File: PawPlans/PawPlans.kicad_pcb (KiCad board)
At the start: 2 copper layers, 80 x 66 mm, 7 parts

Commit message: Completely revamped the schematic and PCB, cleaned up project files
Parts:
- removed LOAD-CELL1: SEN-13879, Parts:SPARKFUN_SEN-13879
- removed PROXIMITY-SENSOR1: ~, Ultrasonic Sensor HC-SR04:HC-SR04_FOOTPRINT
- added LOADCELL1: ~, SparkFun_HX711_Load_Cell_Amplifier_SEN-13879:SPARKFUN-CONNECTORS_1X05, F.Cu at (83.7, 66.3)
- added PROXIMITY1: ~, Ultrasonic_Proximity_Sensor_HC-SR04:HC-SR04_FOOTPRINT, F.Cu at (115.8, 66.0)
- BUZZER1: footprint Parts:XTAL_PS1240P02BT_TDK -> TDK_Piezo_Buzzer_PS1240P02BT:XTAL_PS1240P02BT_TDK
- DISPLAY1: renamed from OLED-BREAKOUT1; footprint Qwiic_OLED_1.3in:SPARKX_1X04_NO_SILK -> SparkFun_Qwiic_OLED_128x64_LCD-23453:SPARKX_1X04
- JOYSTICK1: footprint Parts:1X05 -> Adafruit_Joystick_512:PINHEAD_1X05
- MCUKIT1: renamed from WIFI-DEVKIT1; footprint Espressif:ESP32-C6-DevKitC-1 -> Espressif_ESP32:ESP32-C6-DevKitC-1
- SERVO1: footprint Motors:Vybronics_VZ30C1T8219732L -> Connector_PinHeader_2.00mm:PinHeader_1x03_P2.00mm_Vertical
- moved BUZZER1 98.4 mm to (115.6, 36.8)
- moved MCUKIT1 69.2 mm to (88.2, 43.8)
- moved JOYSTICK1 68.9 mm to (115.7, 53.0), turned to -90 degrees
- moved DISPLAY1 58.5 mm to (83.7, 52.1), turned to 90 degrees
- moved SERVO1 48.6 mm to (115.7, 74.0)
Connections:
- net Net-(OLED-BREAKOUT1-SCL) renamed /DSPSCL
- net Net-(OLED-BREAKOUT1-SDA) renamed /DSPSDA
- BUZZER1 pad 1: Net-(WIFI-DEVKIT1-GPIO12/USB_D-) -> /PZOSIG
- JOYSTICK1 pad 2: Net-(WIFI-DEVKIT1-GPIO16/U0TXD) -> /JOYX
- JOYSTICK1 pad 3: Net-(WIFI-DEVKIT1-GPIO17/U0RXD) -> /JOYY
- JOYSTICK1 pad 4: Net-(WIFI-DEVKIT1-GPIO15/JTAG) -> /JOYSEL
- MCUKIT1 pad 12: Net-(SERVO1-PWM) -> unconnected-(MCUKIT1-GPIO2-Pad12)
- MCUKIT1 pad 19: Net-(WIFI-DEVKIT1-GPIO12/USB_D-) -> unconnected-(MCUKIT1-GPIO12/USB_D--Pad19)
- MCUKIT1 pad 20: Net-(WIFI-DEVKIT1-GPIO13/USB_D+) -> unconnected-(MCUKIT1-GPIO13/USB_D+-Pad20)
- MCUKIT1 pad 22: Net-(WIFI-DEVKIT1-GPIO9/BOOT) -> /SRVPWM
- MCUKIT1 pad 24: unconnected-(WIFI-DEVKIT1-GPIO19-Pad24) -> /PRXTRG
- MCUKIT1 pad 25: unconnected-(WIFI-DEVKIT1-GPIO20-Pad25) -> /PRXECH
- MCUKIT1 pad 26: unconnected-(WIFI-DEVKIT1-GPIO21-Pad26) -> /JOYSEL
- MCUKIT1 pad 27: unconnected-(WIFI-DEVKIT1-GPIO22-Pad27) -> /JOYY
- MCUKIT1 pad 28: unconnected-(WIFI-DEVKIT1-GPIO23-Pad28) -> /JOYX
- MCUKIT1 pad 29: Net-(WIFI-DEVKIT1-GPIO15/JTAG) -> unconnected-(MCUKIT1-GPIO15/JTAG-Pad29)
- MCUKIT1 pad 30: Net-(WIFI-DEVKIT1-GPIO17/U0RXD) -> unconnected-(MCUKIT1-GPIO17/U0RXD-Pad30)
- MCUKIT1 pad 31: Net-(WIFI-DEVKIT1-GPIO16/U0TXD) -> /PZOSIG
- MCUKIT1 pad 6: Net-(LOAD-CELL1-CLK) -> /LDCCLK
- MCUKIT1 pad 7: Net-(LOAD-CELL1-DAT) -> /LDCDAT
- SERVO1 pad 1: Net-(SERVO1-PWM) -> /SRVPWM
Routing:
- net Net-(WIFI-DEVKIT1-GPIO15/JTAG): track 13.0 -> 0.00 mm
- net /PZOSIG: track 0.00 -> 11.5 mm
- net Net-(WIFI-DEVKIT1-GPIO13/USB_D+): track 10.5 -> 0.00 mm
- net Net-(LOAD-CELL1-CLK): track 10.2 -> 0.00 mm
- net Net-(WIFI-DEVKIT1-GPIO17/U0RXD): track 9.42 -> 0.00 mm
- net Net-(SERVO1-PWM): track 9.19 -> 0.00 mm
- net /VCC: track 59.8 -> 51.5 mm
- net /DSPSDA: track 14.0 -> 6.26 mm
- net Net-(WIFI-DEVKIT1-GPIO12/USB_D-): track 7.55 -> 0.00 mm
- net Net-(WIFI-DEVKIT1-GPIO9/BOOT): track 6.97 -> 0.00 mm
- net Net-(WIFI-DEVKIT1-GPIO16/U0TXD): track 6.89 -> 0.00 mm
- net /SRVPWM: track 0.00 -> 6.69 mm
- net /JOYX: track 0.00 -> 6.15 mm
- net /JOYY: track 0.00 -> 6.15 mm
- net /JOYSEL: track 0.00 -> 6.15 mm
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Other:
- board size 80 x 66 mm -> 48 x 68 mm

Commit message: Added board title and credits to silkscreen
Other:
- board text added: "PawPlans - Automatic Pet Feeder v0.5.0 Sriram Vishnubhotla, Logan Swoyer, Jacob Sorber Clemson University"
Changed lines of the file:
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@@
 		(layer "Edge.Cuts")
+	)
+	(gr_text "PawPlans - Automatic Pet Feeder v0.5.0\nSriram Vishnubhotla, Logan Swoyer, Jacob Sorber\nClemson University"
+		(at 89.6 31.2 0)
+		(layer "F.SilkS")
+		(effects
+			(font
+				(size 0.5 0.5)
+				(thickness 0.0625)
+			)
+		)
 	)
 	(segment

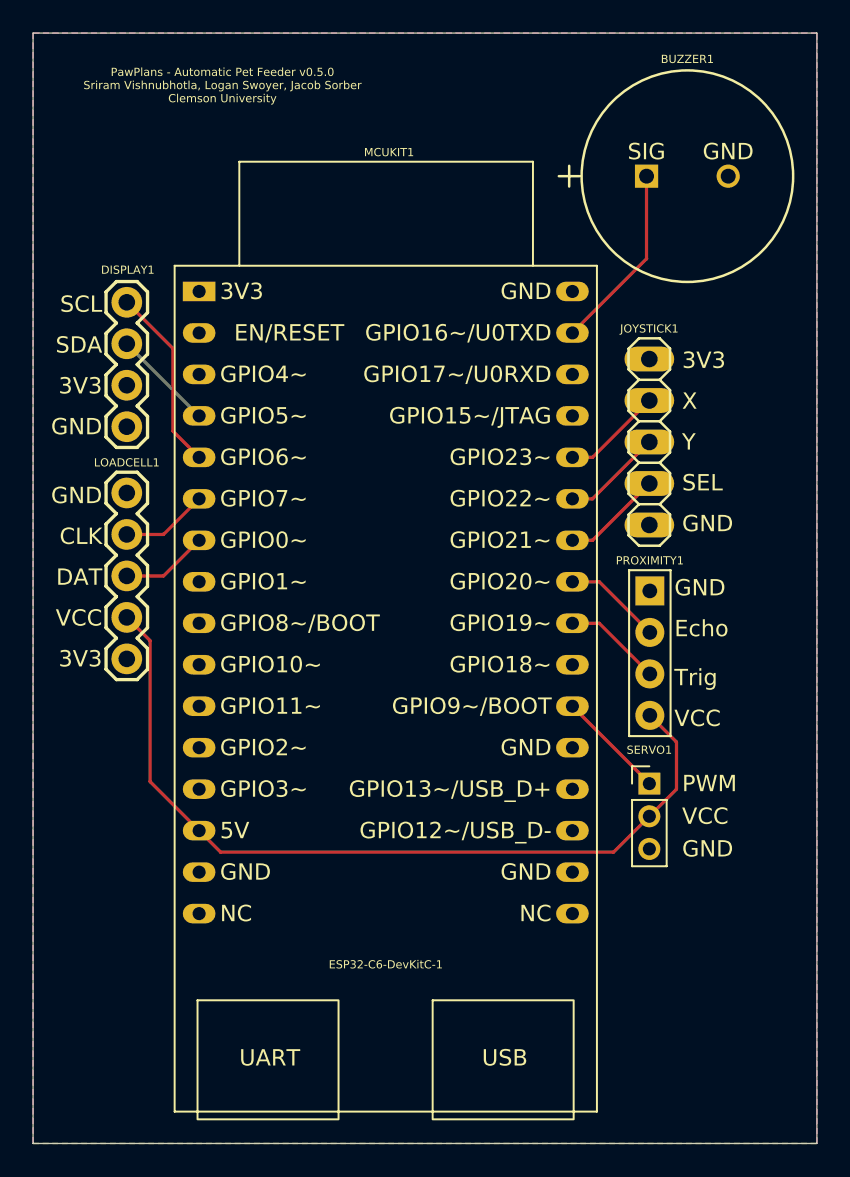
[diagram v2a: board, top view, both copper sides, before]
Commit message: Adjusted the board, switched TDK piezo buzzer for a Murata
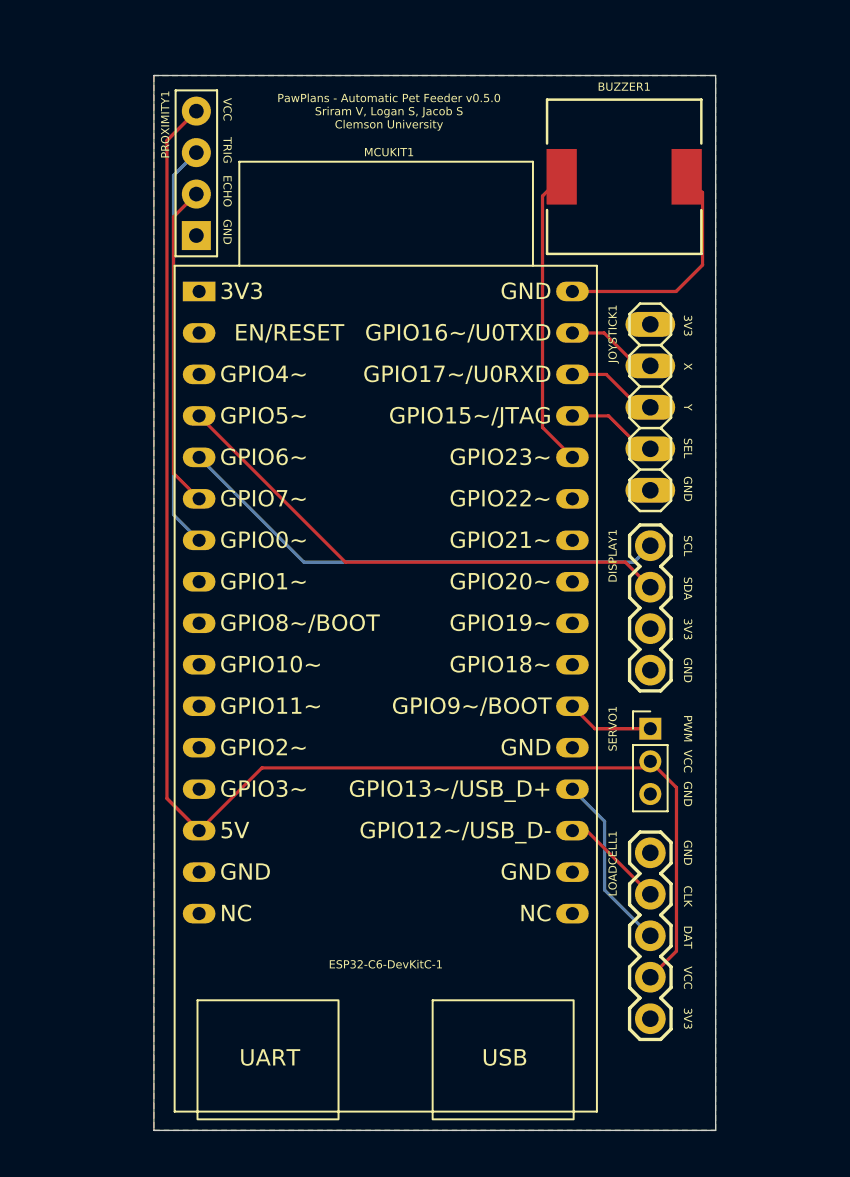
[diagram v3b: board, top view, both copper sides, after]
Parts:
- BUZZER1: value PS1240P02BT -> PKMCS0909E4000-R1; footprint TDK_Piezo_Buzzer_PS1240P02BT:XTAL_PS1240P02BT_TDK -> Murata_SMD_Buzzer_PKMCS0909E4000-R1:PKMCS0909E4000-R1_MUR
- moved PROXIMITY1 40.4 mm to (88.0, 36.6), turned to 180 degrees
- moved LOADCELL1 38.9 mm to (115.8, 88.4)
- moved DISPLAY1 35.4 mm to (115.8, 67.0)
- moved SERVO1 3.36 mm to (115.8, 70.6)
- moved JOYSTICK1 2.12 mm to (115.8, 50.9)
- moved BUZZER1 1.37 mm to (114.2, 36.8)
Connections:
- BUZZER1 pad 1: /PZOSIG -> /BZRSIG
- MCUKIT1 pad 19: unconnected-(MCUKIT1-GPIO12/USB_D--Pad19) -> /LDCCLK
- MCUKIT1 pad 20: unconnected-(MCUKIT1-GPIO13/USB_D+-Pad20) -> /LDCDAT
- MCUKIT1 pad 24: /PRXTRG -> unconnected-(MCUKIT1-GPIO19-Pad24)
- MCUKIT1 pad 25: /PRXECH -> unconnected-(MCUKIT1-GPIO20-Pad25)
- MCUKIT1 pad 26: /JOYSEL -> unconnected-(MCUKIT1-GPIO21-Pad26)
- MCUKIT1 pad 27: /JOYY -> unconnected-(MCUKIT1-GPIO22-Pad27)
- MCUKIT1 pad 28: /JOYX -> /BZRSIG
- MCUKIT1 pad 29: unconnected-(MCUKIT1-GPIO15/JTAG-Pad29) -> /JOYSEL
- MCUKIT1 pad 30: unconnected-(MCUKIT1-GPIO17/U0RXD-Pad30) -> /JOYY
- MCUKIT1 pad 31: /PZOSIG -> /JOYX
- MCUKIT1 pad 6: /LDCCLK -> /PRXECH
- MCUKIT1 pad 7: /LDCDAT -> /PRXTRG
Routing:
- net /VCC: track 51.5 -> 89.0 mm
- net /DSPSDA: track 6.26 -> 32.0 mm
- net /DSPSCL: track 11.3 -> 30.7 mm
- net /PRXTRG: track 6.02 -> 25.0 mm
- net /BZRSIG: track 0.00 -> 18.4 mm
- net /PRXECH: track 6.02 -> 19.9 mm
- net /GND: track 0.00 -> 13.3 mm
- net /PZOSIG: track 11.5 -> 0.00 mm
- net /LDCDAT: track 5.33 -> 11.0 mm
- net /SRVPWM: track 6.69 -> 5.34 mm
- net /JOYX: track 6.15 -> 5.61 mm
- net /JOYY: track 6.15 -> 5.61 mm
- net /JOYSEL: track 6.15 -> 5.61 mm
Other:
- board size 48 x 68 mm -> 34.4 x 64.6 mm
- board text added: "PawPlans - Automatic Pet Feeder v0.5.0 Sriram V, Logan S, Jacob S Clemson University"
- board text removed: "PawPlans - Automatic Pet Feeder v0.5.0 Sriram Vishnubhotla, Logan Swoyer, Jacob Sorber Clemson University"

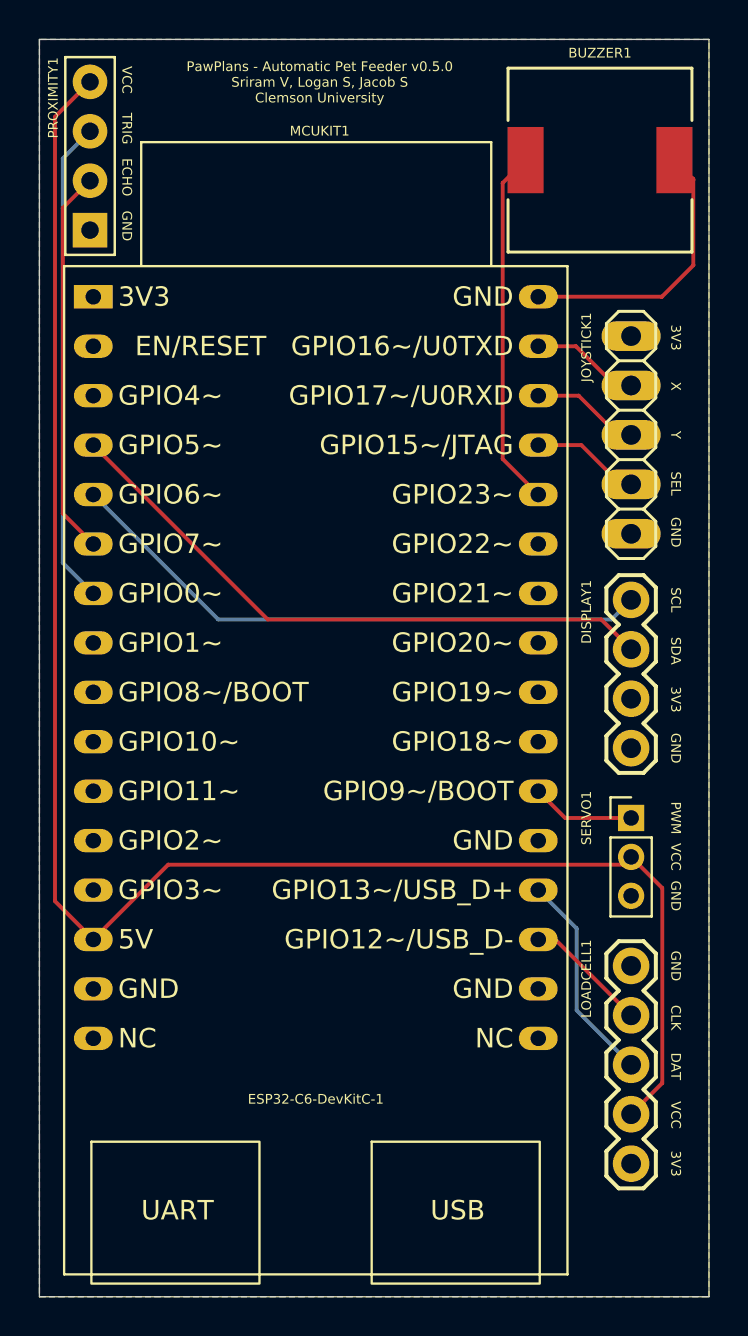
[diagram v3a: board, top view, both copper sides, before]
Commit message: Reworked hardware (centered around M5Stack's DinMeter, ESP32), adjusted board and schematic
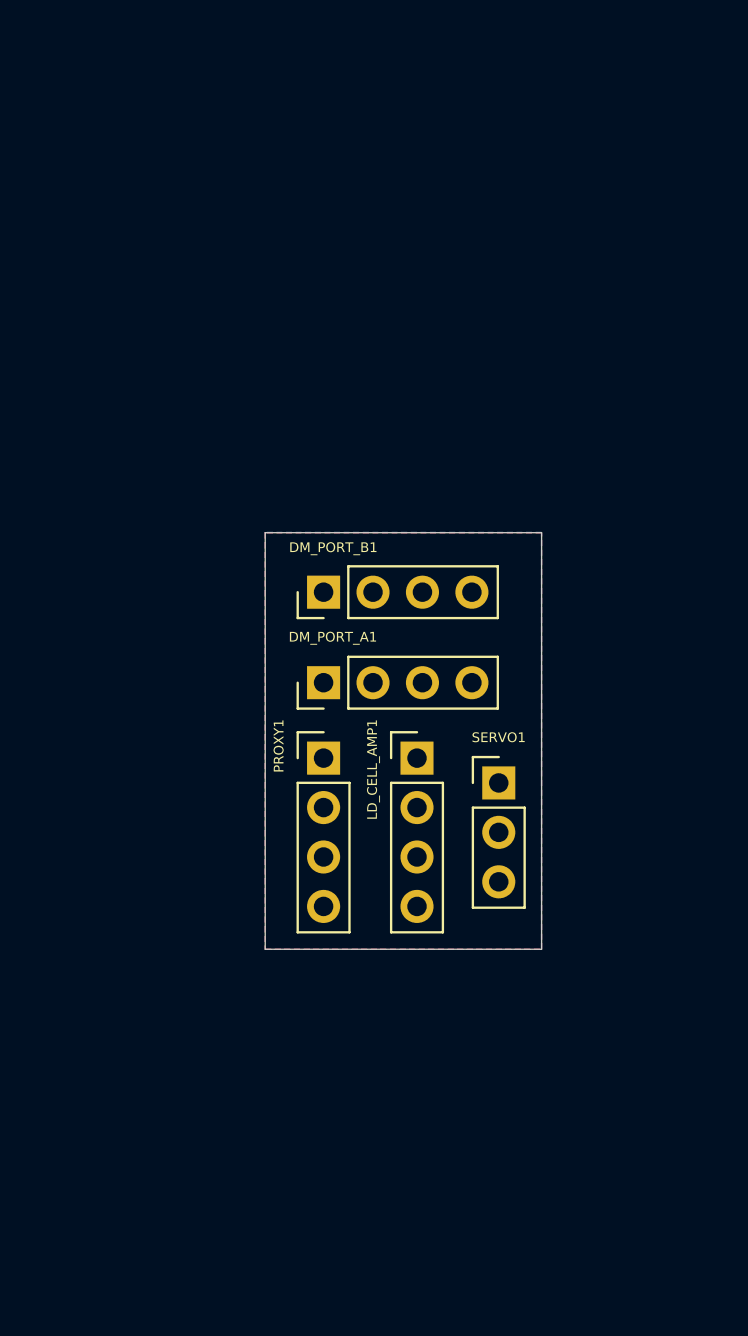
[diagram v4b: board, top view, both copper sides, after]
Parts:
- removed BUZZER1: PKMCS0909E4000-R1, Murata_SMD_Buzzer_PKMCS0909E4000-R1:PKMCS0909E4000-R1_MUR
- removed DISPLAY1: ~, SparkFun_Qwiic_OLED_128x64_LCD-23453:SPARKX_1X04
- removed JOYSTICK1: JOYSTICK-512, Adafruit_Joystick_512:PINHEAD_1X05
- removed LOADCELL1: ~, SparkFun_HX711_Load_Cell_Amplifier_SEN-13879:SPARKFUN-CONNECTORS_1X05
- removed MCUKIT1: ESP32-C6-DevKitC-1, Espressif_ESP32:ESP32-C6-DevKitC-1
- removed PROXIMITY1: ~, Ultrasonic_Proximity_Sensor_HC-SR04:HC-SR04_FOOTPRINT
- added DM_PORT_A1: Conn_01x04, Connector_PinHeader_2.54mm:PinHeader_1x04_P2.54mm_Vertical, F.Cu at (100.0, 63.6)
- added DM_PORT_B1: Conn_01x04, Connector_PinHeader_2.54mm:PinHeader_1x04_P2.54mm_Vertical, F.Cu at (100.0, 59.0)
- added LD_CELL_AMP1: Conn_01x04, Connector_PinHeader_2.54mm:PinHeader_1x04_P2.54mm_Vertical, F.Cu at (104.8, 67.5)
- added PROXY1: Conn_01x04, Connector_PinHeader_2.54mm:PinHeader_1x04_P2.54mm_Vertical, F.Cu at (100.0, 67.5)
- SERVO1: value Motor_Servo -> Conn_01x03; footprint Connector_PinHeader_2.00mm:PinHeader_1x03_P2.00mm_Vertical -> Connector_PinHeader_2.54mm:PinHeader_1x03_P2.54mm_Vertical
- moved SERVO1 7.03 mm to (109.0, 68.8)
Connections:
- SERVO1 pad 1: /SRVPWM -> unconnected-(SERVO1-SGN-Pad1)
- SERVO1 pad 2: /VCC -> /5V
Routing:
- net /VCC: track 89.0 -> 0.00 mm
- net /DSPSDA: track 32.0 -> 0.00 mm
- net /DSPSCL: track 30.7 -> 0.00 mm
- net /PRXTRG: track 25.0 -> 0.00 mm
- net /PRXECH: track 19.9 -> 0.00 mm
- net /BZRSIG: track 18.4 -> 0.00 mm
- net /GND: track 13.3 -> 0.00 mm
- net /LDCDAT: track 11.0 -> 0.00 mm
- net /JOYY: track 5.61 -> 0.00 mm
- net /JOYX: track 5.61 -> 0.00 mm
- net /JOYSEL: track 5.61 -> 0.00 mm
- net /LDCCLK: track 5.51 -> 0.00 mm
- net /SRVPWM: track 5.34 -> 0.00 mm
- added copper zone on F.Cu, net /5V
- removed copper zone on F.Cu, net /3V3
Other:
- board size 34.4 x 64.6 mm -> 14.2 x 21.4 mm
- board text added: "PawPlans - Automatic Pet Feeder Sriram V, Logan S, Jacob S Clemson University"
- board text removed: "PawPlans - Automatic Pet Feeder v0.5.0 Sriram V, Logan S, Jacob S Clemson University"
